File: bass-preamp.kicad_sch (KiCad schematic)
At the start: 26 parts, among them J1 Input, U1 OPA2134, U2 OPA2134

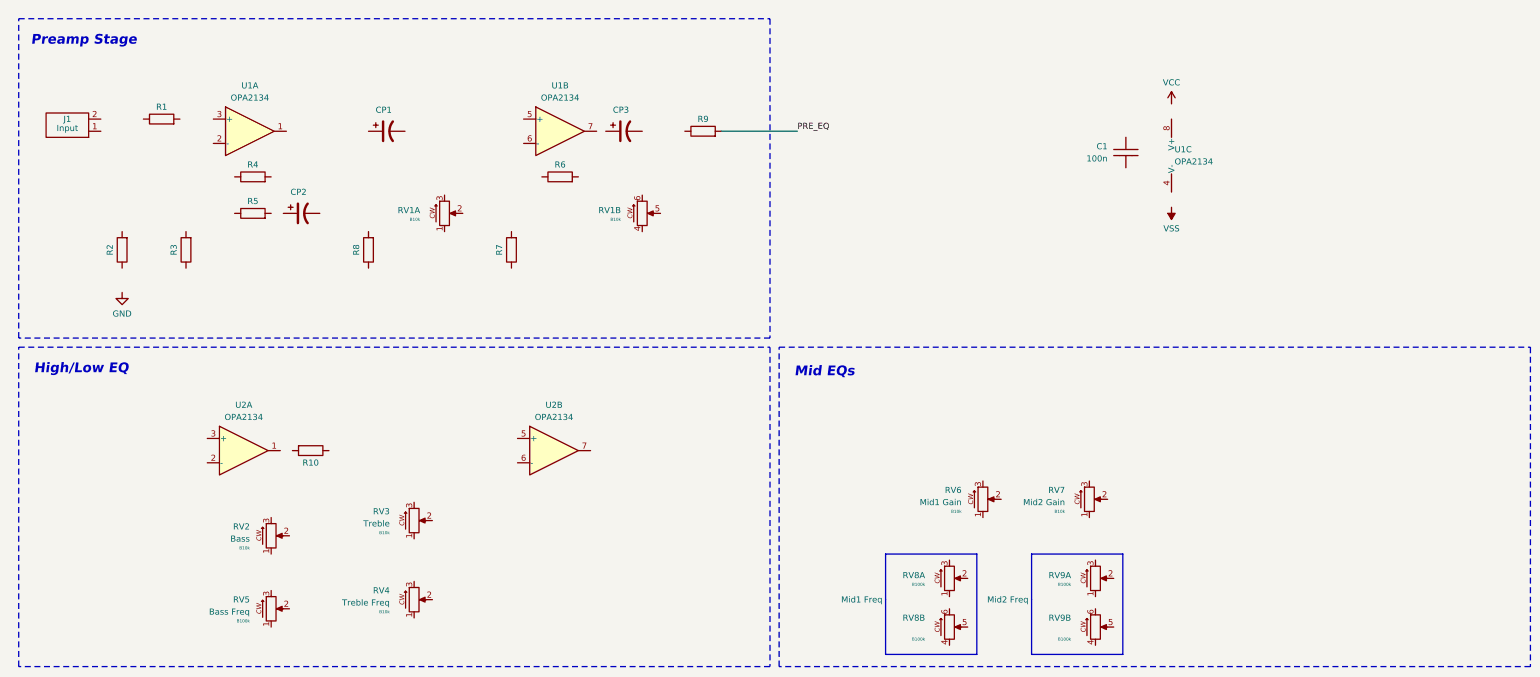
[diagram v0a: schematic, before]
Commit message: more work on schematic and location of pots on board
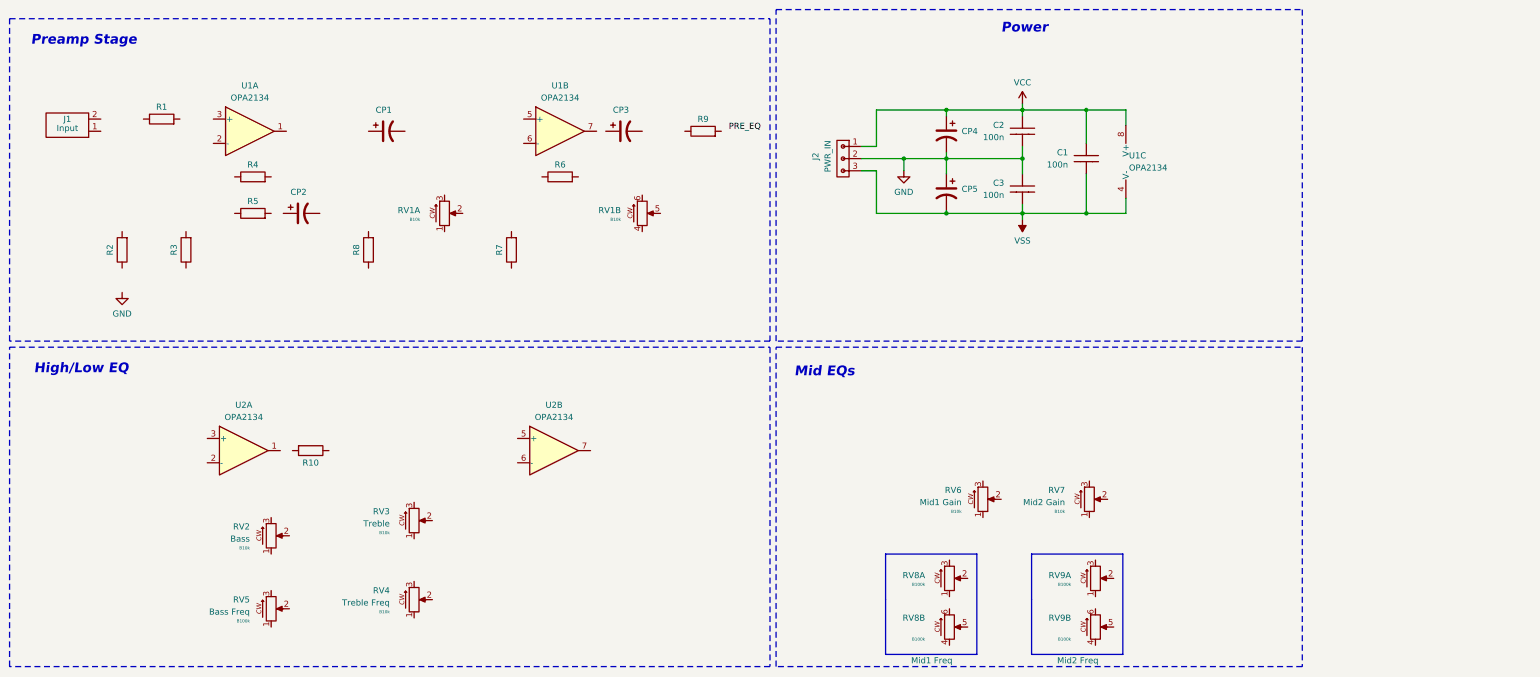
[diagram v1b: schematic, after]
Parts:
- added C2, C3: 3010_Capacitor_0.1uF_25V_THT, Shulltronics_Generics:C_Radial_2.54mm_Vert, symbol Shulltronics_Passives:3010_Capacitor_0.1uF_25V_THT
- added CP4, CP5: 3069_Cap_2.2uF_35V, Shulltronics_Generics:CP_Radial_D3mm_P2mm_Vert, symbol Shulltronics_Passives:3069_Cap_2.2uF_35V
- added J2: PWR_IN, Shulltronics_Connectors:3030_Molex_SL_3pos_Vert, symbol Shulltronics_Connectors:3030_Connector_SL_3pos_Vert
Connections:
- net GND: now also C2.2, C3.1, CP4.2, CP5.1, J2.2
- net PRE_EQ: no longer R9.2
- net VCC: now also C1.1, U1.8 (V+), C2.1, CP4.1, J2.1
- net VSS: now also C1.2, U1.4 (V-), C3.2, CP5.2, J2.3
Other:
- note added: "Power"
- moved on the sheet: C1, U1C
